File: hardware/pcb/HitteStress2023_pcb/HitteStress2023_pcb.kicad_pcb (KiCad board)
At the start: 2 copper layers, 152.4 x 63.5 mm, 10 parts, among them J1 Conn_01x02_Socket, J2 Conn_01x02_Socket, J3 SMA_conector_female, U1 MINIDCDCBOOST5V, U2 TTGO T-Beam T22 V1.1

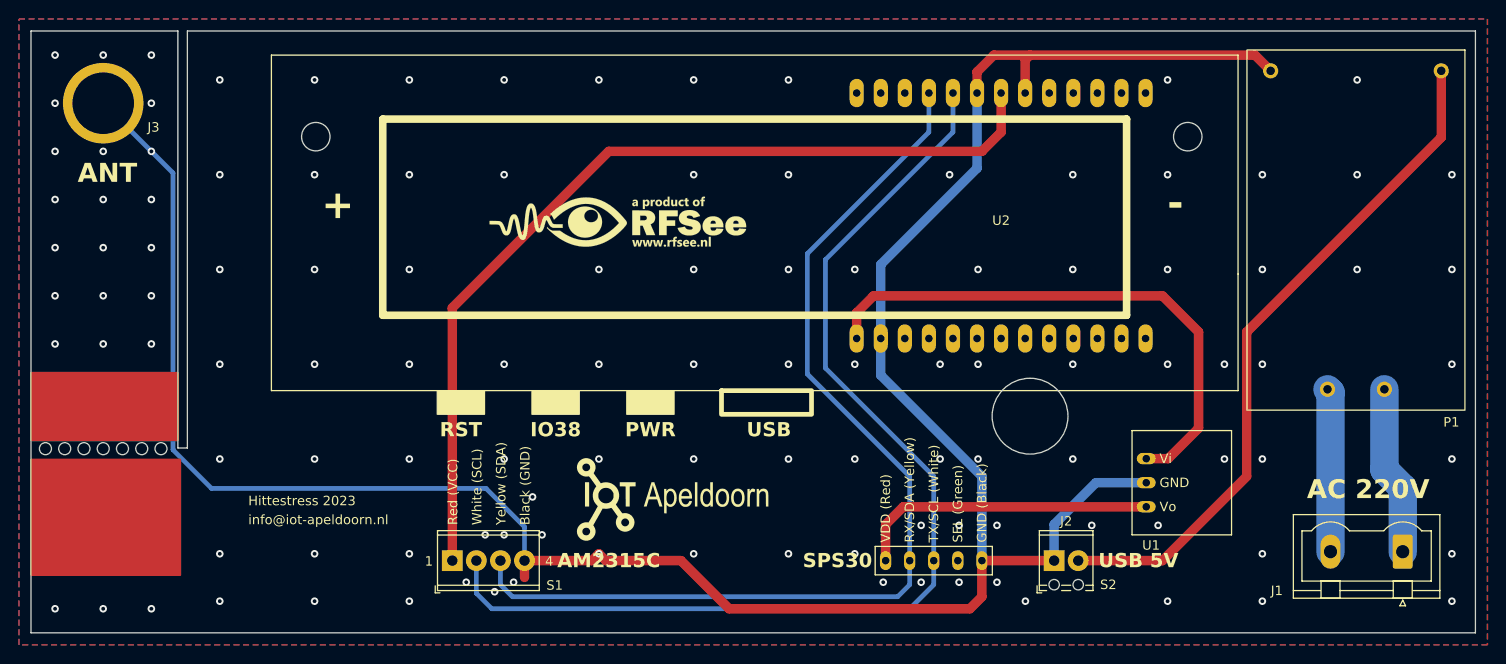
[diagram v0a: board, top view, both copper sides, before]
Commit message: Verified and updated to v0.9 for first prototype print and ordered it.
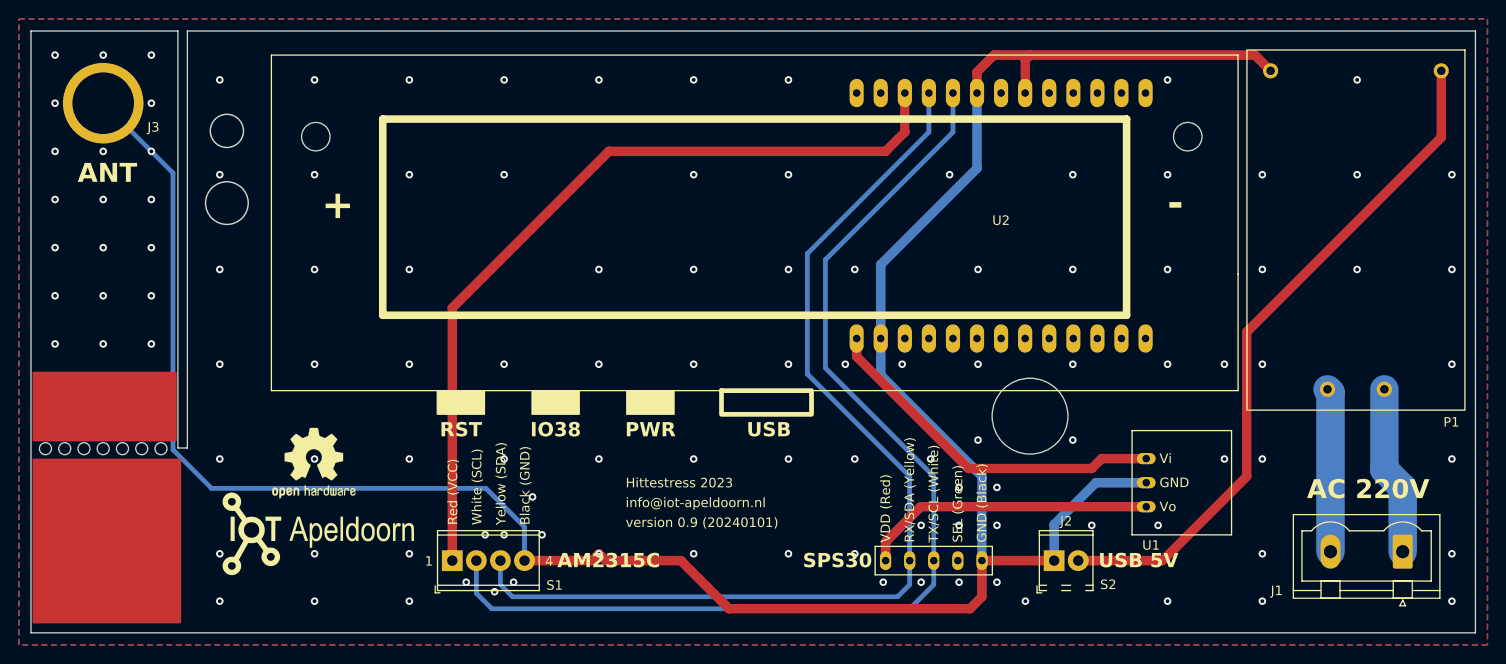
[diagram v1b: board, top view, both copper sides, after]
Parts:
- removed the G*** at (140.7, 55.7)
- added G***: LOGO_LogoRFSee_37x8mm, my-KiCad-library:LOGO_LogoRFSee_37x8mm, F.Cu at (160.7, 56.8)
- added REF**: OSHW-Logo2_9.8x8mm_SilkScreen, Symbol:OSHW-Logo2_9.8x8mm_SilkScreen, F.Cu at (108.6, 81.2)
- added REF**: KiCad-Logo2_8mm_SilkScreen, Symbol:KiCad-Logo2_8mm_SilkScreen, F.Cu at (128.3, 54.9)
- U2: value TTGO T-Beam T22 V1.1 -> TTGO_T-Beam_T22_V1.1
- moved G*** 37.6 mm to (108.7, 88.7)
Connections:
- U2 pad 16: unconnected-(U2-3V3-Pad16) -> /3V3
- U2 pad 20: /3V3 -> unconnected-(U2-3V3-Pad20)
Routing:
- net /5V_U: track 58.1 -> 37.8 mm
- net /3V3: track 96.4 -> 86.2 mm
- net /GND: track 260.5 -> 258.7 mm, vias 118 -> 117
- net /5V_SPS: track 32.1 -> 31.0 mm
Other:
- outline, holes or cut-outs redrawn
- board text added: "version 0.9 (20240101)"

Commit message: Version 1.0 after prototype soldering
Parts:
- removed the REF** at (108.6, 81.2)
- added REF**: OSHW-Logo2_14.6x12mm_SilkScreen, Symbol:OSHW-Logo2_14.6x12mm_SilkScreen, F.Cu at (113.7, 80.0)
- J1: footprint Connector_Phoenix_GMSTB:PhoenixContact_GMSTBVA_2,5_2-G-7,62_1x02_P7.62mm_Vertical -> Connector_Phoenix_MC_HighVoltage:PhoenixContact_MCV_1,5_2-G-5.08_1x02_P5.08mm_Vertical
- J2: footprint my-KiCad-library:TerminalBlock_Phoenix_MPT-0,5-2-2.54_1x02_P2.54mm_Horizontal -> TerminalBlock_Phoenix:TerminalBlock_Phoenix_MPT-0,5-2-2.54_1x02_P2.54mm_Horizontal
- moved J1 2.51 mm to (221.0, 90.2)
- moved G*** 1.29 mm to (161.9, 56.5)
- moved REF** 0.32 mm to (128.3, 55.2)
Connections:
- S2 pad 4: unconnected-(S2-SEL-Pad4) -> /GND
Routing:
- net Net-(J1-Pin_1): track 17.9 -> 17.0 mm
- net /GND: vias 117 -> 116
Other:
- board text added: "version 1.0 (20240108)"
- board text removed: "version 0.9 (20240101)"

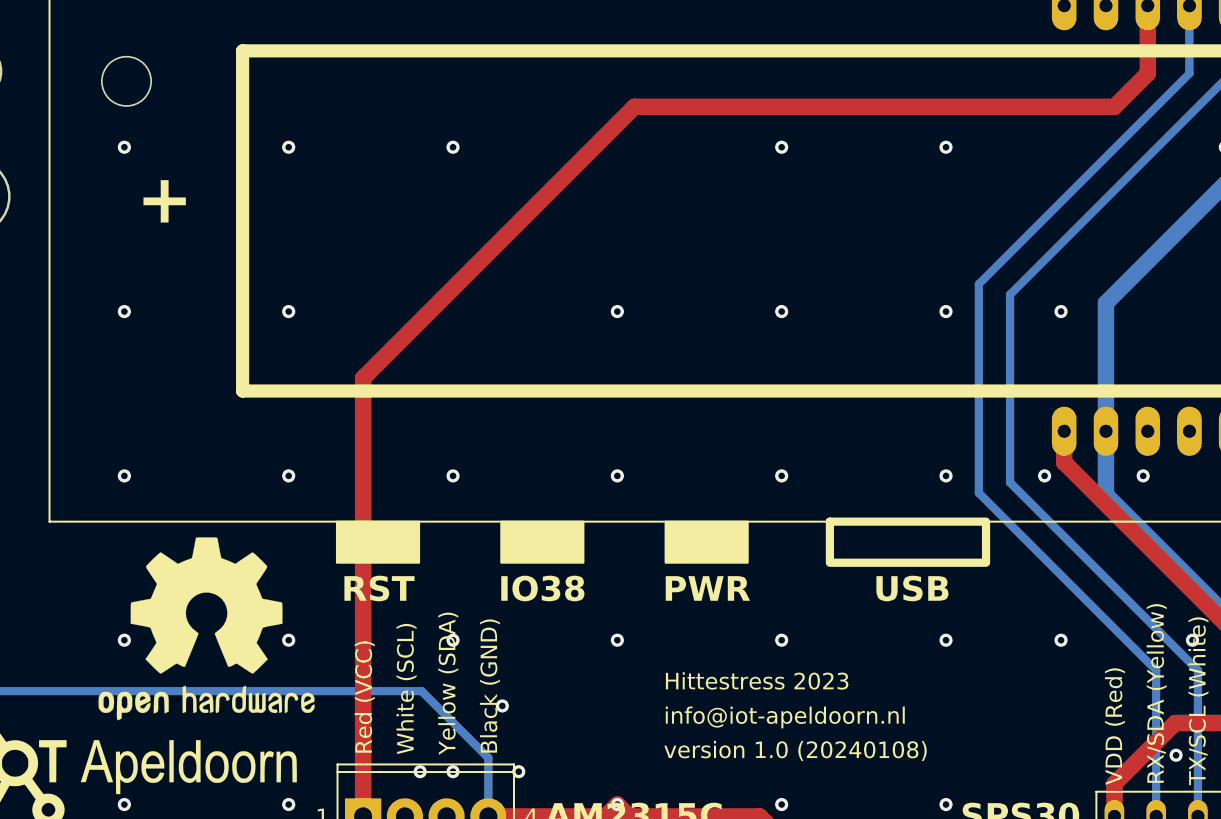
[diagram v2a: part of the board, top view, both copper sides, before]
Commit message: Added 2x pull-pup resistors for I2C
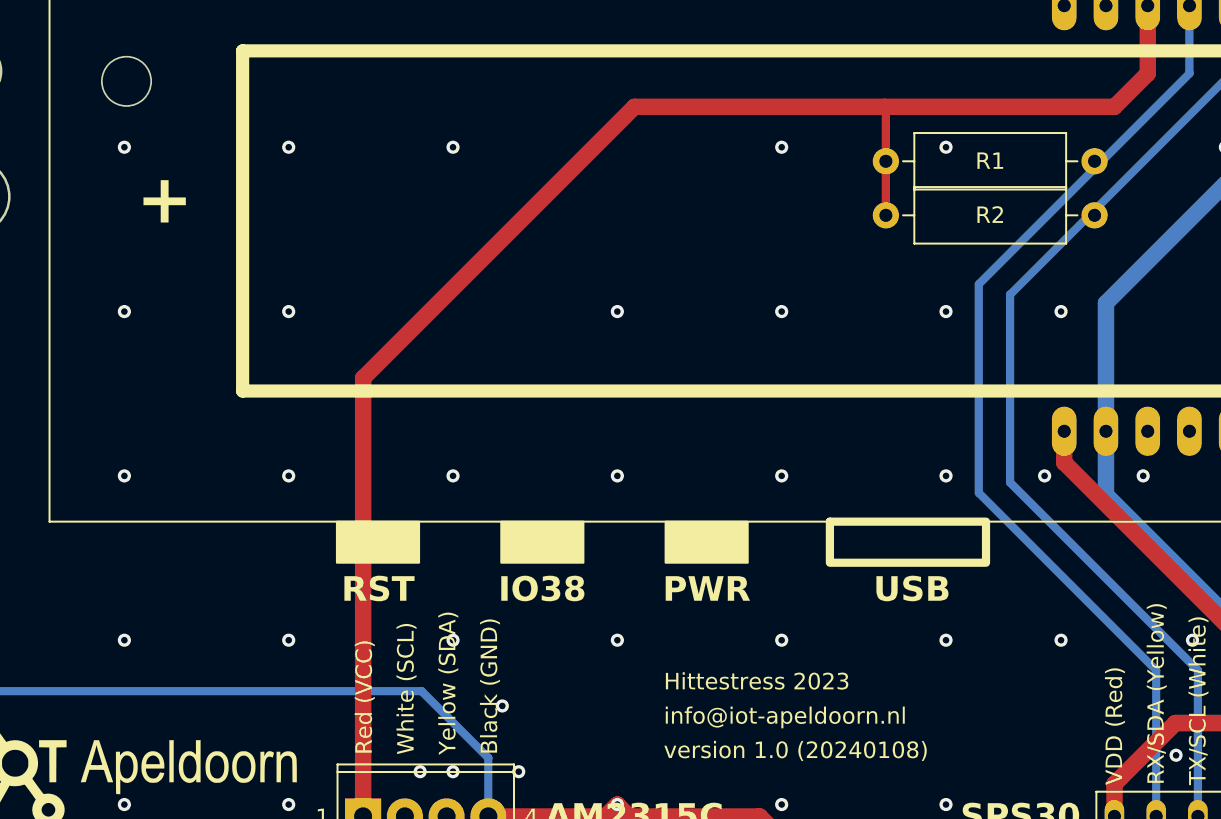
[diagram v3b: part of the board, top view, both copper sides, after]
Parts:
- removed the G*** at (161.9, 56.5)
- removed REF**: KiCad-Logo2_8mm_SilkScreen, Symbol:KiCad-Logo2_8mm_SilkScreen
- removed REF**: OSHW-Logo2_14.6x12mm_SilkScreen, Symbol:OSHW-Logo2_14.6x12mm_SilkScreen
- added R1: 10K, Resistor_THT:R_Axial_DIN0309_L9.0mm_D3.2mm_P12.70mm_Horizontal, F.Cu at (155.0, 51.6)
- added R2: 10K, Resistor_THT:R_Axial_DIN0309_L9.0mm_D3.2mm_P12.70mm_Horizontal, F.Cu at (155.0, 54.9)
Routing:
- net /3V3: track 86.2 -> 92.9 mm
